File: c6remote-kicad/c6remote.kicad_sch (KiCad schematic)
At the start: 34 parts, among them J1 Battery, Q1 MMBT2222A, SW1 SW_Push, SW10 SW_Push, SW11 SW_Push, SW2 SW_Push, SW3 SW_Push, SW4 SW_Push, SW5 SW_Push, SW6 SW_Push, SW7 SW_Push, SW8 SW_Push, SW9 SW_Push, U1 XIAO-ESP32-C6, U2 TSOP4136, U3 PCF8575DBR

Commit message: feat(led): swap D2-D5 to XINGLIGHT XL-2020RGBC-WS2812B on a datasheet-correct land pattern, LCSC C5349955 with 183k stock and cheaper than the discontinued C965555 it replaces - rated VDD 3.5-5.5V not 3.7-5.3V, VIH 0.5*VDD not an absolute 2.7V, and 5mA/ch not 12mA so blue Vf headroom improves on the under-spec 3.3V rail (roughly 3x dimmer, fine for state display); new Library footprint LED_XL-2020RGBC-WS2812B_PLCC4_2.0x2.0mm puts 0.85x0.75mm pads at +/-0.675 X and +/-0.625 Y where the stock 2.2x2.0 body part had 0.7x0.7 at +/-0.915 and +/-0.55 (old pads overlapped only about 59% of the new terminals, biased outboard), with silk +/-1.3/+/-1.2 and courtyard +/-1.35/+/-1.25 both tighter in X than the part they replace; footprint positions, rotations, uuids, path, pinfunctions and all 16 pad nets preserved, and every signal and power stub still terminates inside its new pad so nothing needed rerouting; all four VSS pads gain zone_connect 2 for a solid pour connection after the smaller pads starved D5 pad 2 to 1 thermal spoke against a min of 2, which is locally overridden to error rather than warning; pin numbering is identical (1 DO, 2 GND, 3 DI, 4 VDD) per the DigiKey-hosted datasheet revision, whose pin table the xonstorage revision contradicts, so no net remap and lib_id stays LED:WS2812B-2020; c6remote.yaml unchanged since the protocol is still WS2812 GRB 800kHz reset >100us; Mouser and Adafruit sourcing fields dropped as neither carries the part; ERC 0, DRC 48 pre-existing silk/lib warnings 0 errors 0 unconnected, parity 13 board-only TP_* only, BOM regroups to one row qty 4
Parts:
- D2, D3, D4, D5: value WS2812B-2020 -> XL-2020RGBC-WS2812B; footprint LED_SMD:LED_WS2812B-2020_PLCC4_2.0x2.0mm -> Library:LED_XL-2020RGBC-WS2812B_PLCC4_2.0x2.0mm; Adafruit https://www.adafruit.com/product/4684 -> (none); Digikey https://www.digikey.com/en/products/detail/adafruit-industr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 -> https://www.digikey.com/en/products/detail/xinglight/XL-202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; LCSC https://www.lcsc.com/product-detail/C965555.html -> https://www.lcsc.com/product-detail/C5349955.html; MPN WS2812B-2020 -> XL-2020RGBC-WS2812B; Manufacturer Worldsemi -> XINGLIGHT; Mouser https://www.mouser.com/ProductDetail/Adafruit/4684 -> (none)

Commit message: fix(mic): renumber the ICS-43434 symbol pins to the datasheet so MK1 is wired correctly, the embedded INMP441_Microphone_I2S symbol and its project-local inmp441_microphone_i2s.kicad_sym source both carried INMP441 numbering of 1 SCK, 2 WS, 3 L/R, 4 SD, 5 VDD, 6 GND against the ICS-43434 truth in DS-000069 v1.2 Table 8 of 1 WS, 2 LR, 3 GND, 4 SCK, 5 VDD, 6 SD, which put the 3.072MHz bit clock on the mic WS pin, the 48kHz frame clock on LR, left the real SCK pin floating on the undriven sd net and soldered the SD output straight into the GND pour, explaining the bring-up result of 100% zero samples at the correct 192000 B/s byte rate on both channel settings since a mic clocked under 200kHz sits in standby with SD tristated while the ESP samples its own high-Z clock input; the stock Sensor_Audio footprint was already correct with pad N equal to physical pin N, verified against datasheet Fig 3 and Fig 15, so only the symbol changed, pin positions and electrical types untouched so every wire endpoint and net-to-function pairing is preserved; board updated from the schematic with MK1 rotated 180 to 0 in place and the mic cluster rerouted, pads now ws on 1, GND on 2 and 3, sck on 4, +3.3V on 5 and sd on 6, tracks going 289 to 319 segments and 2082.025mm to 2081.778mm with footprints unchanged at 47 and pads at 170, the acoustic NPTH moving to (53.35, 31.582) and the front silk mic ring following to (53.35, 31.575); zones refilled in the GUI and verified current, a pcbnew ZONE_FILLER pass on a copy reproduces the stored fills exactly with area delta 0 on the GND and +3.3V pours; validated ERC 0, DRC 43 violations 0 errors 0 unconnected parity 13 with the type breakdown back at baseline 24 silk_over_copper, 14 lib_footprint_mismatch, 4 silk_edge_clearance and 1 silk_overlap; docs/mic-bringup.md records the root cause and marks the continuity checks superseded because the fault is netlist-level, not assembly
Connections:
- net GND: now also MK1.2 (L/R); no longer MK1.6 (GND)
- net sck: now also MK1.4 (SCK); no longer MK1.1 (SCK)
- net sd: now also MK1.6 (SD), U1.4 (GPIO21_D3); no longer MK1.4 (SD), U1.1 (GPIO0_A0_D0)
- net ws: now also MK1.1 (WS), U1.1 (GPIO0_A0_D0); no longer MK1.2 (WS), U1.4 (GPIO21_D3)

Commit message: feat(led): gate the D2-D5 rail with a high-side P-FET so the four XL-2020RGBC-WS2812B stop burning ~2.4mA quiescent while dark, which was the binding constraint on battery life since a WS2812-class controller die stays powered and listening whenever VDD is present and writing all channels to zero only zeroes PWM duty; Q2 AO3401A (SOT-23, Alpha and Omega, LCSC C15127) puts source on +3.3V, drain on the new led_vdd net feeding all four VDD pads and gate on the new led_en net, with R10 1M pulling the gate to the source so the rail is off by default because GPIO18 boots as a floating input, and Rds(on) 60 milliohm gives 22mV of drop at the 60mA full-white peak; led_en lands on U1 pad 11 (GPIO18/D10), the last unconnected XIAO edge pad, and TP_GPIO18_D10_MOSI now probes it, leaving GPIO6 pad 29 and GPIO7 pad 25 as the only spares; kept high-side so all four LED VSS pads stay zone_connect 2 in the F.Cu GND pour, and the four +3.3V vias that dropped each VDD pad into the B.Cu plane are removed in favour of a led_vdd tree of 39.3mm F.Cu plus 51.9mm B.Cu with 4 vias; C4 1uF 50V X7R 0805 added mid-chain on led_vdd because that plane drop was the whole reason the chain previously needed no decoupling, and it reuses C1's MPN so the BOM groups them into one line; the first routing attempt ran led_vdd diagonally across F.Cu past the wheel and severed the GND pour neck, orphaning D5 VSS in a 77mm2 island as DRC's only unconnected item, so that branch moved to B.Cu and the pour is now 2 islands at 2364.9 and 735.9mm2 with all four LED VSS pads in the main one while the B.Cu +3.3V plane stays a single island at 3348.5mm2; ERC 0, DRC 0 errors and 0 unconnected with the inherited 43 silkscreen and library warnings, parity 13 extra_footprint for the TP_* test points
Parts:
- added C4: 1uF, Capacitor_SMD:C_0805_2012Metric, symbol Device:C
- added Q2: AO3401A, Package_TO_SOT_SMD:SOT-23, symbol Transistor_FET:AO3401A
- added R10: 1M, Resistor_SMD:R_0603_1608Metric, symbol Device:R
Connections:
- net +3.3V: now also Q2.2 (S), R10.1; no longer D2.4 (VDD), D3.4 (VDD), D4.4 (VDD), D5.4 (VDD)
- net GND: now also C4.2
- net led_en: now reaches U1.11 (GPIO18_D10_MOSI)
- net led_en: now also Q2.1 (G), R10.2
- new net led_vdd: C4.1, D2.4 (VDD), D3.4 (VDD), D4.4 (VDD), D5.4 (VDD), Q2.3 (D)
- no-connect marks 6 -> 5
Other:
- moved on the sheet: D2, D3, D4

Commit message: fix(pcb): give D1 a forked horizontal footprint with + and - silk glyphs, since the part is a 3mm IR LED whose leads bend 90 degrees to aim out the top board edge but the board drew it standing upright, and the pad shapes had just been swapped in place so the instance no longer matched LED_THT and DRC sat at 44 warnings; kicad lib/Library.pretty/LED_D3.0mm_Horizontal_O1.27mm_Z2.0mm_IRBlack.kicad_mod forks the stock horizontal variant, which needs no copper change because its pads are the same 1.8mm at (0,0) and (2.54,0), keeps pad 1 circle for the cathode and pad 2 square for the anode as chosen so the square reads as positive, adds 0.9mm + and - glyphs beside the anode and cathode at global (60.2, 30.6) and (65.4, 30.6), and trims the silk body to a base line plus two stubs ending at local y 3.4, which is global 28.875 and 0.66mm clear of the top edge at 28.214, because the real 3mm body overhangs that edge by about 2.6mm and the untrimmed outline would have added silk_edge_clearance violations and been clipped out of the gerbers anyway; the full lying-down body, the dome arc and the courtyard stay on F.Fab and F.CrtYd where no edge rule applies, so the mechanical extent is still documented; the 3D model was already the horizontal Z2.0mm step, so renders and STEP were right while the drawn geometry was wrong, and the two now agree; only the D1 symbol instance carries the new Library: link because editing the schematic's embedded lib_symbols copy raises lib_symbol_mismatch in ERC; zones refilled and saved in the GUI after the pad shape change altered the pour cutouts, F.Cu GND still 2 islands at 2362.8 and 735.9mm2 and the B.Cu +3.3V plane still one at 3348.1mm2; ERC 0, DRC 43 warnings at the inherited breakdown of 24 silk_over_copper, 14 lib_footprint_mismatch, 4 silk_edge_clearance and 1 silk_overlap with D1 no longer among the mismatches, 0 errors, 0 unconnected, parity 13 extra_footprint for the TP_* test points; kicad_pro default pad size drift reverted again
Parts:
- D1: footprint LED_THT:LED_D3.0mm_IRBlack -> Library:LED_D3.0mm_Horizontal_O1.27mm_Z2.0mm_IRBlack
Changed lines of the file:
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@@
 			)
 		)
-		(property "Footprint" "LED_THT:LED_D3.0mm_IRBlack"
+		(property "Footprint" "Library:LED_D3.0mm_Horizontal_O1.27mm_Z2.0mm_IRBlack"
 			(at 161.29 33.655 0)
 			(hide yes)

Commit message: fix(pcb): rework the board for PCBWay's second via-in-pad report, delete all 14 TP_* test points, retire the VCC rail, and bump the front silk to 2026.8.0, taking DRC to 1 warning and schematic parity to 0; PCBWay reported vias in pad against the newer files, which does not reproduce, so scripts/check-via-in-pad.py now sweeps every via centre plus annular ring against every pad rectangle layer-agnostically and confirms the four originals sit dead centre in R9.1, R9.2, SW11.2 and U3.1 at -0.300mm on 1693423^ while 2026.7.1 and this board have zero overlaps, closest approach 0.305mm at U3 pin 1, so their marked-up file is what is needed to close it out; board side, vias moved clear, tracks tidied, vias 24 to 33 and segments 343 to 355, R8 moved from 51.415,152.75 rot 180 to 52.75,153.25 rot -90, the 14 TP_* footprints deleted, which also clears the silk_overlap warning and the 13 extra_footprint parity issues, and VCC is retired because it had shrunk to the U1/14 VBUS node alone, so the schematic pin now carries a no-connect and the board reads unconnected-(U1-VBUS-Pad14); ERC 0, DRC 0 errors and 0 unconnected with only the U1 lib_footprint_mismatch left, parity 0, zones reproduce their stored fill to 0.0000mm2 so the GUI refill is saved, position file still 35 rows with 0 test points and BOM output byte-identical to 2026.7.1, the answer PCBWay asked for; docs follow the new baseline, and AGENTS.md now says power splits two ways with no probe pad on any signal
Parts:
- removed TP_VCC1: TestPoint_THTPad_1.0x1.0mm_Drill0.5mm_NoCrtYd, Local:TestPoint_THTPad_1.0x1.0mm_Drill0.5mm_NoCrtYd, symbol Connector:TestPoint
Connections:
- net VCC: no longer names the net of U1.14 (VBUS)
- no-connect marks 5 -> 6
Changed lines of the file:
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@@
 	)
 	(no_connect
+		(at 236.22 85.09)
+	)
+	(no_connect
 		(at 205.74 66.04)
 	)
@@
 		)
 	)
-	(global_label "VCC"
-		(shape bidirectional)
-		(at 236.22 85.09 0)
-		(effects
-			(font
-				(size 1.27 1.27)
-			)
-			(justify left)
-		)
-		(property "Intersheetrefs" "${INTERSHEET_REFS}"
-			(at 236.22 85.09 0)
-			(hide yes)
-			(show_name no)
-			(do_not_autoplace no)
-			(effects
-				(font
-					(size 1.27 1.27)
-				)
-			)
-		)
-	)
 	(global_label "ano_sw5"
 		(shape input)
@@
 		)
 	)
-	(global_label "VCC"
-		(shape bidirectional)
-		(at 240.03 72.39 270)
-		(fields_autoplaced yes)
-		(effects
-			(font
-				(size 1.27 1.27)
-			)
-			(justify right)
-		)
-		(property "Intersheetrefs" "${INTERSHEET_REFS}"
-			(at 240.03 80.1151 90)
-			(hide yes)
-			(show_name no)
-			(do_not_autoplace no)
-			(effects
-				(font
-					(size 1.27 1.27)
-				)
-				(justify right)
-			)
-		)
-	)
 	(global_label "sw9"
 		(shape input)
@@
 		(pin "2"
 		)
-		(instances)
+		(instances
+			(project "c6remote"
+				(path "/0cbb6fa3-42c1-48e5-afd9-e4923c6691f6"
+					(reference "C4")
+					(unit 1)
+				)
+			)
+		)
 	)
 	(symbol
@@
 	)
 	(symbol
-		(lib_id "Connector:TestPoint")
-		(at 240.03 72.39 0)
-		(unit 1)
-		(body_style 1)
-		(exclude_from_sim no)
-		(in_bom no)
-		(on_board yes)
-		(in_pos_files no)
-		(dnp no)
-		(fields_autoplaced yes)
-		(property "Reference" "TP_VCC1"
-			(at 242.57 71.12 0)
-			(show_name no)
-			(do_not_autoplace no)
-			(effects
-				(font
-					(size 1.27 1.27)
-				)
-				(justify left)
-			)
-		)
-		(property "Value" "TestPoint_THTPad_1.0x1.0mm_Drill0.5mm_NoCrtYd"
-			(at 242.57 73.66 0)
-			(hide yes)
-			(show_name no)
-			(do_not_autoplace no)
-			(effects
-				(font
-					(size 1.27 1.27)
-				)
-				(justify left)
-			)
-		)
-		(property "Footprint" "Local:TestPoint_THTPad_1.0x1.0mm_Drill0.5mm_NoCrtYd"
-			(at 240.03 72.39 0)
-			(hide yes)
-			(show_name no)
-			(do_not_autoplace no)
-			(effects
-				(font
-					(size 1.27 1.27)
-				)
-			)
-		)
-		(property "Datasheet" ""
-			(at 240.03 72.39 0)
-			(hide yes)
-			(show_name no)
-			(do_not_autoplace no)
-			(effects
-				(font
-					(size 1.27 1.27)
-				)
-			)
-		)
-		(property "Description" ""
-			(at 240.03 72.39 0)
-			(hide yes)
-			(show_name no)
-			(do_not_autoplace no)
-			(effects
-				(font
-					(size 1.27 1.27)
-				)
-			)
-		)
-		(pin "1"
-		)
-		(instances
-			(project "c6remote"
-				(path "/0cbb6fa3-42c1-48e5-afd9-e4923c6691f6"
-					(reference "TP_VCC1")
-					(unit 1)
-				)
-			)
-		)
-	)
-	(symbol
 		(lib_id "power:GND")
 		(at 45.72 35.56 180)
@@
 		(pin "1"
 		)
-		(instances)
+		(instances
+			(project "c6remote"
+				(path "/0cbb6fa3-42c1-48e5-afd9-e4923c6691f6"
+					(reference "#PWR043")
+					(unit 1)
+				)
+			)
+		)
 	)
 	(sheet_instances
@@
 		)
 	)
+	(embedded_fonts no)
 )

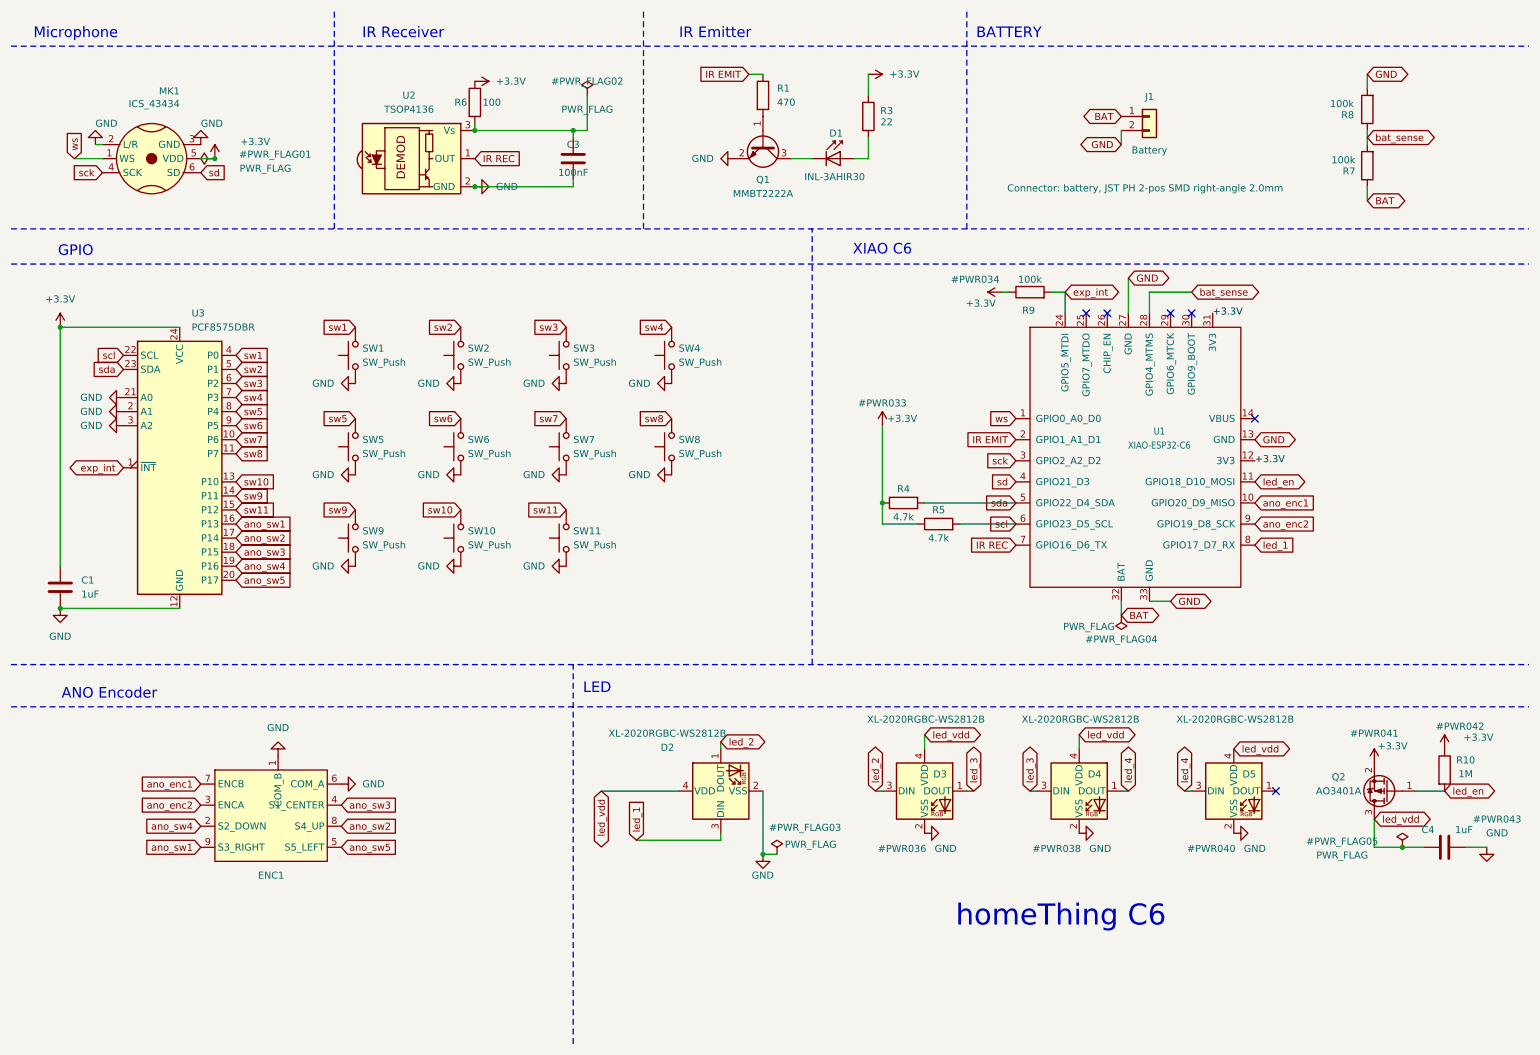
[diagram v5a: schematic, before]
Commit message: feat(pcb): gate the IR receiver rail behind Q3 and R11 on a new ir_vdd net with ir_en on GPIO6, taking the deep-sleep floor from ~0.41mA to ~58uA and standby on a 1000mAh cell from 82 days to 575, because U2 was 88% of the standby draw at 350uA continuous while listening for something that cannot wake the board, IR REC sitting on GPIO16 outside the C6's GPIO0-GPIO7 wake range; Q3 is a second AO3401A with source on +3.3V and drain on ir_vdd, R11 a 1M gate pull-up holding the rail off by default, and R6's upper end moves off +3.3V so the gate sits upstream of the existing R6/C3 filter, which stays with U2 untouched and is why no reservoir cap is needed unlike C4 on the LED rail; Q3 and R11 sit beside U1 rather than U2, the opposite of Q2, because ir_en is a 1M high-impedance node whenever GPIO6 is an input so the whole net is kept short while ir_vdd takes the 110mm run at 350uA of DC for 0.2mV of drop; the first routing attempt pinched the F.Cu GND pour into unreachable pieces, the same trap led_vdd hit, fixed with stitching vias so the pour is now 3 mutually reachable regions of 1882.9, 695.6 and 375.8mm2 against a single 3220.8mm2 B.Cu +3.3V plane; firmware gains an IR Rail switch on GPIO6, inverted like led_rail but ALWAYS_ON rather than ALWAYS_OFF since remote_receiver cannot decode with U2 unpowered and switching it off while awake only leaks ~44uA back through GPIO16's pullup into U2's internal 30k, so the saving is real only in deep sleep where the pullup is released; ERC 0, DRC 1 warning (the inherited U1 lib_footprint_mismatch), 0 unconnected and parity 0, all four ESPHome configs valid, position file 37 rows and the BOM groups Q3 with Q2 and R11 with R10; silk stays 2026.8.1, which is exactly what the next push to main computes; docs add the board's first power budget with datasheet currents for every always-on part, and AGENTS.md now bans the MCP sync_schematic_to_board outright after it corrupted 16 existing pad nets, including rotating MK1 1/2/4/6 back in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
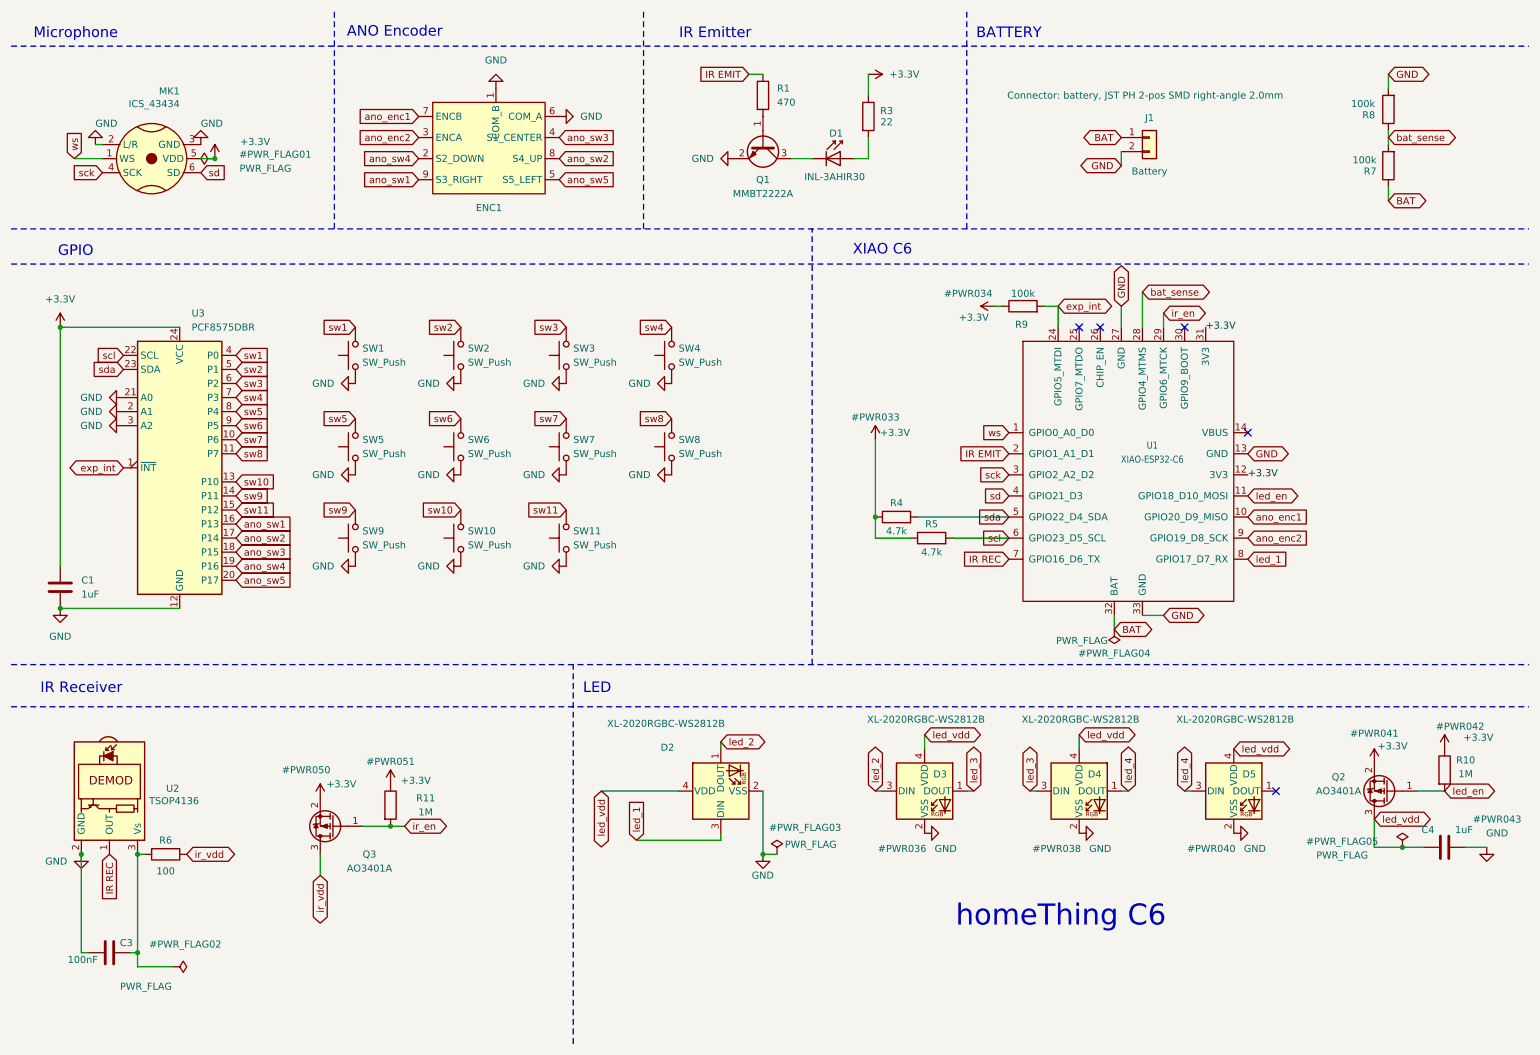
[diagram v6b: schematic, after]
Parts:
- added Q3: AO3401A, Package_TO_SOT_SMD:SOT-23, symbol Transistor_FET:AO3401A
- added R11: 1M, Resistor_SMD:R_0603_1608Metric, symbol Device:R
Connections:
- net +3.3V: now also Q3.2 (S), R11.1; no longer R6.1
- net ir_en: now reaches U1.29 (GPIO6_MTCK)
- net ir_en: now also Q3.1 (G), R11.2
- new net ir_vdd: Q3.3 (D), R6.1
- no-connect marks 6 -> 5
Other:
- moved on the sheet: C3, ENC1, J1, R4, R5, R6, R7, R8, R9, U1, U2
